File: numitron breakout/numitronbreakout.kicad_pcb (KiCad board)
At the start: 4 copper layers, 60 x 100 mm, 18 parts, among them J1 Conn_01x06, M3 SCREW MountingHole_3.2mm_M3_Pad, U1 HV5812WG-G, U2 LM317_TO-220, U3 LM317_TO-220, U4 IV-12, U5 IV-12

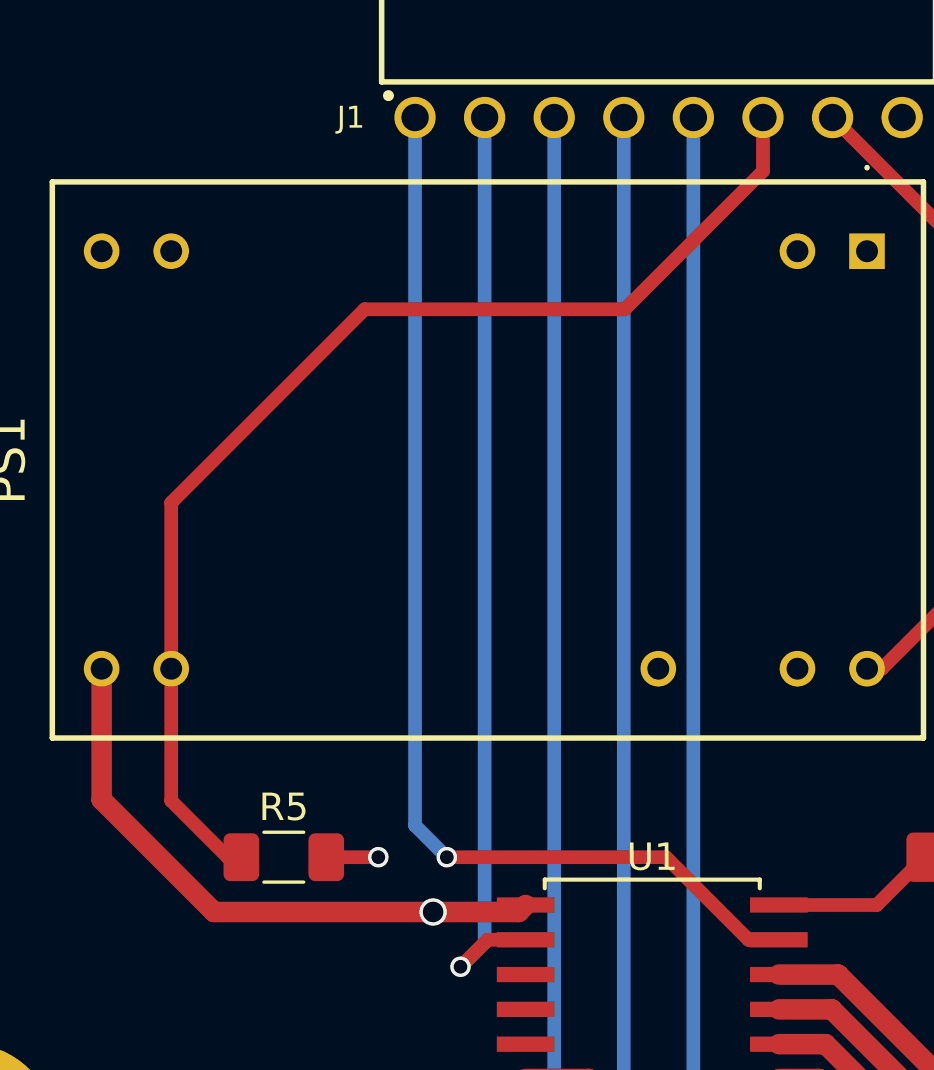
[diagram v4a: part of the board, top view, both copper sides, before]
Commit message: fixed dimming issue
dimming pwm signal was connected to the wrong pin (VOUT2 instead of PWM_DIM) on the meanwell power supply.
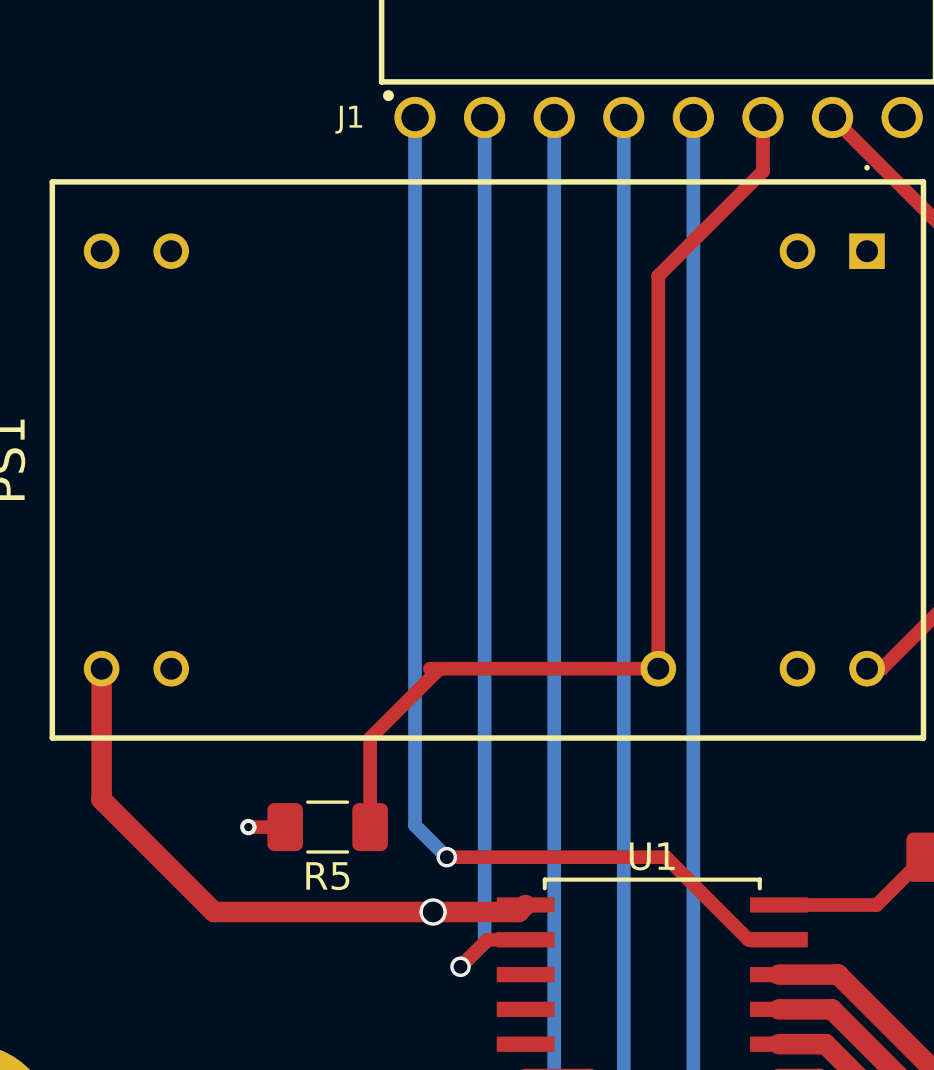
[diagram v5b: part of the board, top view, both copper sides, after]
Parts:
- moved R5 1.94 mm to (138.2, 88.9), turned to 180 degrees
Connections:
- PS1 pad 14: DIMMING -> unconnected-(PS1-+VOUT_2-Pad14)
- PS1 pad 21: unconnected-(PS1-PWM_DIM-Pad21) -> DIMMING
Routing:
- net DIMMING: track 42.9 -> 36.9 mm
- net GND: track 8.82 -> 8.27 mm
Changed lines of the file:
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@@
 	)
 	(paper "A4")
+	(title_block
+		(rev "1")
+	)
 	(layers
 		(0 "F.Cu" signal)
@@
 			(psa4output no)
 			(plot_black_and_white yes)
+			(plotinvisibletext no)
 			(sketchpadsonfab no)
 			(plotpadnumbers no)
@@
 	(net 32 "Net-(U1-HVOUT4)")
 	(net 33 "Net-(U1-HVOUT15)")
-	(net 34 "unconnected-(PS1-PWM_DIM-Pad21)")
+	(net 34 "unconnected-(PS1-+VOUT_2-Pad14)")
 	(net 35 "unconnected-(PS1-+VIN_1-Pad23)")
 	(net 36 "unconnected-(PS1--VOUT_2-Pad12)")
@@
 			)
 		)
-		(attr exclude_from_pos_files exclude_from_bom)
+		(attr board_only exclude_from_pos_files exclude_from_bom)
 		(fp_circle
 			(center 0 0)
@@
 			)
 		)
-		(sheetname "Root")
+		(sheetname "/")
 		(sheetfile "numitronbreakout.kicad_sch")
 		(attr exclude_from_bom)
@@
 			)
 		)
-		(attr exclude_from_pos_files exclude_from_bom)
+		(attr board_only exclude_from_pos_files exclude_from_bom)
 		(fp_circle
 			(center 0 0)
@@
 		)
 		(property ki_fp_filters "C_*")
-		(sheetname "Root")
+		(sheetname "/")
 		(sheetfile "numitronbreakout.kicad_sch")
 		(attr smd)
@@
 		)
 		(property ki_fp_filters "SOW28_17P90X7P50_MCH SOW28_17P90X7P50_MCH-M SOW28_17P90X7P50_MCH-L")
-		(sheetname "Root")
+		(sheetname "/")
 		(sheetfile "numitronbreakout.kicad_sch")
 		(attr smd)
@@
 		)
 		(property ki_fp_filters "R_*")
-		(sheetname "Root")
+		(sheetname "/")
 		(sheetfile "numitronbreakout.kicad_sch")
 		(attr smd)
@@
 		)
 		(property ki_fp_filters "R_*")
-		(sheetname "Root")
+		(sheetname "/")
 		(sheetfile "numitronbreakout.kicad_sch")
 		(attr smd)
@@
 	(footprint "Resistor_SMD:R_1206_3216Metric_Pad1.30x1.75mm_HandSolder"
 		(layer "F.Cu")
-		(at 136.55 90)
+		(at 138.15 88.9 180)
 		(descr "Resistor SMD 1206 (3216 Metric), square (rectangular) end terminal, IPC_7351 nominal with elongated pad for handsoldering. (Body size source: IPC-SM-782 page 72, https://www.pcb-3d.com/wordpress/wp-content/uploads/ipc-sm-782a_amendment_1_and_2.pdf), generated with kicad-footprint-generator")
 		(tags "resistor handsolder")
@@
 		)
 		(property "Datasheet" "https://www.vishay.com/docs/20035/dcrcwe3.pdf"
-			(at 0 0 0)
+			(at 0 0 180)
 			(unlocked yes)
 			(layer "F.Fab")
@@
 		)
 		(property "Description" "RES SMD 1K OHM 1% 1/4W 1206"
-			(at 0 0 0)
+			(at 0 0 180)
 			(unlocked yes)
 			(layer "F.Fab")
@@
 		)
 		(property "MFR" "Vishay Dale"
-			(at 0 0 0)
+			(at 0 0 180)
 			(unlocked yes)
 			(layer "F.Fab")
@@
 		)
 		(property "Part No" "CRCW040248R7FKED"
-			(at 0 0 0)
+			(at 0 0 180)
 			(unlocked yes)
 			(layer "F.Fab")
@@
 		)
 		(property "Manufacturer_Name" "Vishay Dale"
-			(at 0 0 0)
+			(at 0 0 180)
 			(unlocked yes)
 			(layer "F.Fab")
@@
 		)
 		(property "Manufacturer_Part_Number" "CRCW12061K00FKEA"
-			(at 0 0 0)
+			(at 0 0 180)
 			(unlocked yes)
 			(layer "F.Fab")
@@
 		)
 		(property ki_fp_filters "R_*")
-		(sheetname "Root")
+		(sheetname "/")
 		(sheetfile "numitronbreakout.kicad_sch")
 		(attr smd)
 		(fp_line
-			(start -0.727064 -0.91)
-			(end 0.727064 -0.91)
+			(start -0.727064 0.91)
+			(end 0.727064 0.91)
 			(stroke
 				(width 0.12)
@@
 		)
 		(fp_line
-			(start -0.727064 0.91)
-			(end 0.727064 0.91)
+			(start -0.727064 -0.91)
+			(end 0.727064 -0.91)
 			(stroke
 				(width 0.12)
@@
 		)
 		(fp_line
-			(start -2.45 -1.12)
-			(end 2.45 -1.12)
+			(start 2.45 1.12)
+			(end -2.45 1.12)
 			(stroke
 				(width 0.05)
@@
 		)
 		(fp_line
-			(start -2.45 1.12)
-			(end -2.45 -1.12)
+			(start 2.45 -1.12)
+			(end 2.45 1.12)
 			(stroke
 				(width 0.05)
@@
 		)
 		(fp_line
-			(start 2.45 -1.12)
-			(end 2.45 1.12)
+			(start -2.45 1.12)
+			(end -2.45 -1.12)
 			(stroke
 				(width 0.05)
@@
 		)
 		(fp_line
-			(start 2.45 1.12)
-			(end -2.45 1.12)
+			(start -2.45 -1.12)
+			(end 2.45 -1.12)
 			(stroke
 				(width 0.05)
@@
 		)
 		(fp_line
-			(start -1.6 -0.8)
-			(end 1.6 -0.8)
+			(start 1.6 0.8)
+			(end -1.6 0.8)
 			(stroke
 				(width 0.1)
@@
 		)
 		(fp_line
-			(start -1.6 0.8)
-			(end -1.6 -0.8)
+			(start 1.6 -0.8)
+			(end 1.6 0.8)
 			(stroke
 				(width 0.1)
@@
 		)
 		(fp_line
-			(start 1.6 -0.8)
-			(end 1.6 0.8)
+			(start -1.6 0.8)
+			(end -1.6 -0.8)
 			(stroke
 				(width 0.1)
@@
 		)
 		(fp_line
-			(start 1.6 0.8)
-			(end -1.6 0.8)
+			(start -1.6 -0.8)
+			(end 1.6 -0.8)
 			(stroke
 				(width 0.1)
@@
 		)
 		(pad "1" smd roundrect
-			(at -1.55 0)
+			(at -1.55 0 180)
 			(size 1.3 1.75)
 			(layers "F.Cu" "F.Mask" "F.Paste")
@@
 		)
 		(pad "2" smd roundrect
-			(at 1.55 0)
+			(at 1.55 0 180)
 			(size 1.3 1.75)
 			(layers "F.Cu" "F.Mask" "F.Paste")
@@
 			)
 		)
-		(attr exclude_from_pos_files exclude_from_bom)
+		(attr board_only exclude_from_pos_files exclude_from_bom)
 		(fp_circle
 			(center 0 0)
@@
 			)
 		)
-		(sheetname "Root")
+		(sheetname "/")
 		(sheetfile "numitronbreakout.kicad_sch")
 		(attr exclude_from_bom)
@@
 			)
 		)
-		(attr exclude_from_pos_files exclude_from_bom)
+		(attr board_only exclude_from_pos_files exclude_from_bom)
 		(fp_circle
 			(center 0 0)
@@
 		)
 		(property ki_fp_filters "Connector*:*_1x??_*")
-		(sheetname "Root")
+		(sheetname "/")
 		(sheetfile "numitronbreakout.kicad_sch")
 		(attr through_hole)
@@
 			)
 		)
-		(sheetname "Root")
+		(sheetname "/")
 		(sheetfile "numitronbreakout.kicad_sch")
 		(attr through_hole)
@@
 			(layers "*.Cu" "*.Mask")
 			(remove_unused_layers no)
-			(net 5 "DIMMING")
+			(net 34 "unconnected-(PS1-+VOUT_2-Pad14)")
 			(pinfunction "+VOUT_2")
 			(pintype "passive")
@@
 			(layers "*.Cu" "*.Mask")
 			(remove_unused_layers no)
-			(net 34 "unconnected-(PS1-PWM_DIM-Pad21)")
+			(net 5 "DIMMING")
 			(pinfunction "PWM_DIM")
 			(pintype "passive")
@@
 		)
 		(property ki_fp_filters "R_*")
-		(sheetname "Root")
+		(sheetname "/")
 		(sheetfile "numitronbreakout.kicad_sch")
 		(attr smd)
@@
 		)
 		(property ki_fp_filters "R_*")
-		(sheetname "Root")
+		(sheetname "/")
 		(sheetfile "numitronbreakout.kicad_sch")
 		(attr smd)
@@
 		)
 		(property ki_fp_filters "TO?220*")
-		(sheetname "Root")
+		(sheetname "/")
 		(sheetfile "numitronbreakout.kicad_sch")
 		(attr through_hole)
@@
 			)
 		)
-		(attr exclude_from_pos_files exclude_from_bom)
+		(attr board_only exclude_from_pos_files exclude_from_bom)
 		(fp_circle
 			(center 0 0)
@@
 		)
 		(property ki_fp_filters "TO?220*")
-		(sheetname "Root")
+		(sheetname "/")
 		(sheetfile "numitronbreakout.kicad_sch")
 		(attr through_hole)
@@
 	)
 	(segment
-		(start 132.44 83.12)
-		(end 132.44 77.06)
-		(width 0.5)
-		(layer "F.Cu")
-		(net 5)
-	)
-	(segment
-		(start 132.44 87.94)
-		(end 134.5 90)
+		(start 150.22 83.12)
+		(end 142.24 83.12)
 		(width 0.5)
 		(layer "F.Cu")
@@
 	)
 	(segment
-		(start 132.44 83.12)
-		(end 132.44 87.94)
+		(start 139.7 85.66)
+		(end 139.7 88.9)
 		(width 0.5)
 		(layer "F.Cu")
@@
 	)
 	(segment
-		(start 134.5 90)
-		(end 135 90)
+		(start 150.22 68.78)
+		(end 150.22 83.12)
 		(width 0.5)
 		(layer "F.Cu")
@@
 	)
 	(segment
-		(start 149 70)
-		(end 154.04 64.96)
+		(start 154.04 64.96)
+		(end 150.22 68.78)
 		(width 0.5)
 		(layer "F.Cu")
@@
 	)
 	(segment
-		(start 132.44 77.06)
-		(end 139.5 70)
+		(start 142.24 83.12)
+		(end 141.88 83.12)
 		(width 0.5)
 		(layer "F.Cu")
@@
 	)
 	(segment
-		(start 139.5 70)
-		(end 149 70)
+		(start 142.24 83.12)
+		(end 139.7 85.66)
 		(width 0.5)
 		(layer "F.Cu")
@@
 	)
 	(segment
-		(start 138.1 90)
-		(end 140 90)
+		(start 136.6 88.9)
+		(end 135.255 88.9)
 		(width 0.5)
 		(layer "F.Cu")
@@
 	)
 	(via
-		(at 143.5 109)
-		(size 0.75)
-		(drill 0.5)
+		(at 135.255 88.9)
+		(size 0.6)
+		(drill 0.3)
 		(layers "F.Cu" "B.Cu")
 		(net 31)
 	)
 	(via
-		(at 140 90)
+		(at 143.5 109)
 		(size 0.75)
 		(drill 0.5)

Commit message: updated breakout board gerbers
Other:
- board text added: "IV-12 NUMITRON DRIVER BOARD A. LEVINE REV.02"
- board text removed: "IV-12 NUMITRON DRIVER BOARD A. LEVINE REV.01"
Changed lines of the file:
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@@
 		)
 	)
-	(gr_text "IV-12 NUMITRON DRIVER BOARD\nA. LEVINE			REV.01"
+	(gr_text "IV-12 NUMITRON DRIVER BOARD\nA. LEVINE			REV.02"
 		(at 150 149.5 0)
 		(layer "F.SilkS")
